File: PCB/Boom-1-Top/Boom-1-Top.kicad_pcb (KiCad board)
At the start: 4 copper layers, 345 x 165 mm, 770 parts, among them J1 DEBUG, J10 PIC_DEBUG, J11 PIC_DEBUG, J12 PIC_DEBUG, J13 PIC_DEBUG, J14 PIC_DEBUG, J15 USB_B_Micro, J16 SD_Card, J17 BT_DEBUG, J18 12V Supply, J19 3V3 Bypass, J2 MIDI IN, J20 5V Bypass, J3 MIDI OUT, J37 Osc1Conn, J38 Osc2Conn, J39 SubNoiseConn, J4 PIC_DEBUG, J40 FiltConn2, J41 EnvGenConn2, J42 EnvGenConn1, J43 FXConn1, J44 FiltConn1, J45 FXConn2, J46 EnvGenConn3, J5 PIC_DEBUG, J6 PIC_DEBUG, J7 PIC_DEBUG, J8 PIC_DEBUG, J9 PIC_DEBUG, Q1 AO3401A, Q2 AO3401A, SW1 Osc1SawEncoder, SW10 SubToOsc2FiltEncoder, SW11 Osc1ToOsc2FiltEncoder, SW12 Osc1FiltFreqEncoder, SW13 Osc2FiltFreqEncoder, SW14 SubFiltFreqEncoder, SW15 OscFiltEnvAttackEncoder, SW16 SubFiltEnvAttackEncoder, SW17 Osc1FiltResEncoder, SW18 Osc2FiltResEncoder, SW19 SubFiltResEncoder, SW2 Osc1SqrEncoder, SW20 OscFiltEnvDecayEncoder, SW21 SubFiltEnvDecayEncoder, SW22 OscFiltEnvSustainEncoder, SW23 SubFiltEnvSustainEncoder, SW24 Osc1DriveEncoder, SW25 Osc2DistortionEncoder, SW26 OscFiltEnvReleaseEncoder, SW27 SubFiltEnvReleaseEncoder, SW28 FXWetDryEncoder, SW29 SubAmpEnvAttackEncoder, SW3 Rotary_Encoder, SW30 OscAmpEnvAttackEncoder, SW31 FXControl1Encoder, SW32 SubAmpEnvDecayEncoder, SW33 OscAmpEnvDecayEncoder, SW34 FXControl2Encoder, SW35 SubAmpEnvSustainEncoder, SW36 OscAmpEnvSustainEncoder, SW37 FXControl3Encoder, SW38 FXFeedbackEncoder, SW39 SubAmpEnvReleaseEncoder, SW4 Rotary_Encoder_Switch, SW40 OscAmpEnvReleaseEncoder, SW41 Reset, SW43 Reset, SW5 Rotary_Encoder, SW53 Osc1TuneEncoder, SW6 SubToSubFiltEncoder, SW7 SubNoiseEncoder, U1 STM32F407VGTx, U10 DAC7678xPW, U11 PIC18F26Q43, U12 PIC18F26Q43, U13 PIC18F26Q43, U14 PIC18F26Q43, U15 PIC18F26Q43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

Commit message: Left-side knobs now all have 22mm spacing between them And 29mm between the groups
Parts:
- moved SW1 1.00 mm to (150.0, 107.2)
- moved SW7 1.00 mm to (150.0, 253.2)
- moved SW2 0.50 mm to (150.0, 129.2)
- moved SW3 0.50 mm to (150.0, 158.2)
- moved SW4 0.50 mm to (150.0, 180.2)
- moved SW5 0.50 mm to (150.0, 202.2)
- moved SW6 0.50 mm to (150.0, 231.2)
- moved SW28 0.20 mm to (378.0, 180.2)
- moved SW31 0.20 mm to (402.0, 180.2)
- moved SW34 0.20 mm to (422.0, 180.2)
- moved SW37 0.20 mm to (442.0, 180.2)

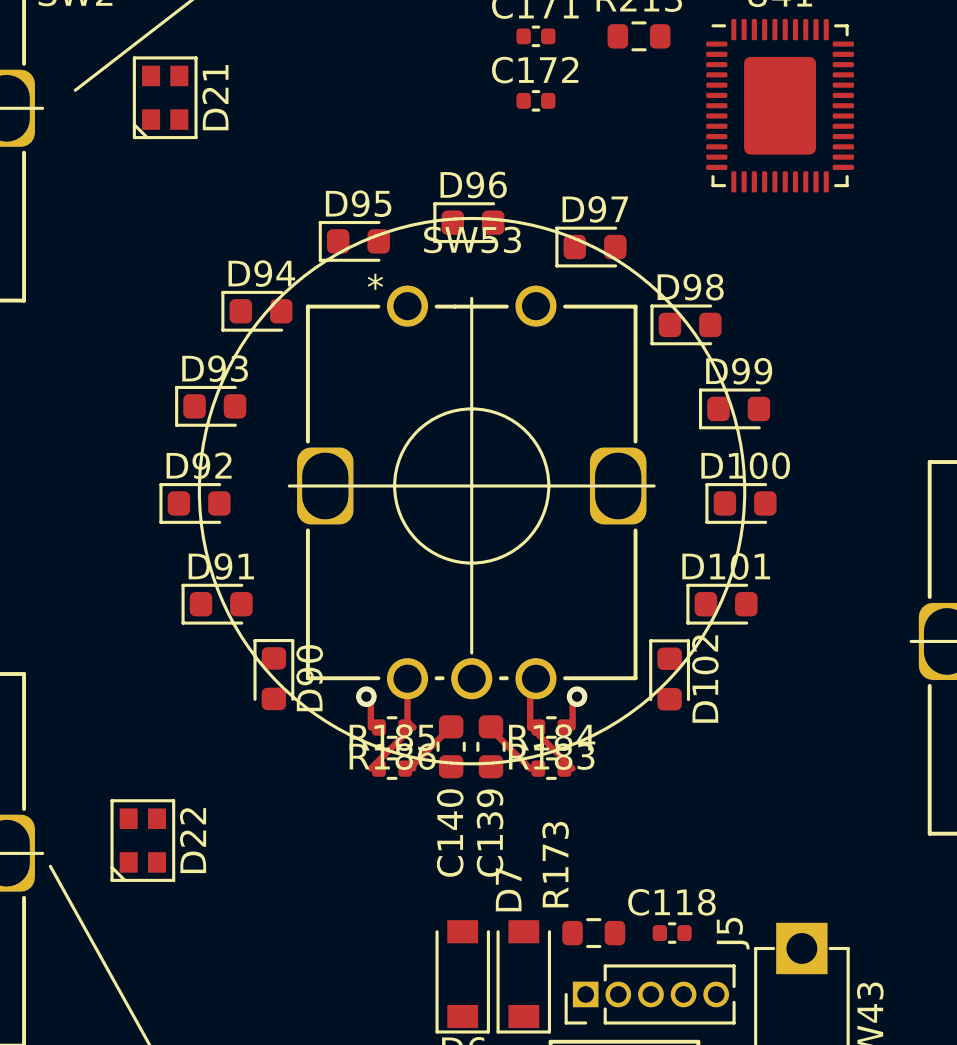
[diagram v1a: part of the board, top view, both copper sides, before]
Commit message: Re-aligned horizontal guide lines Aligned tune knob
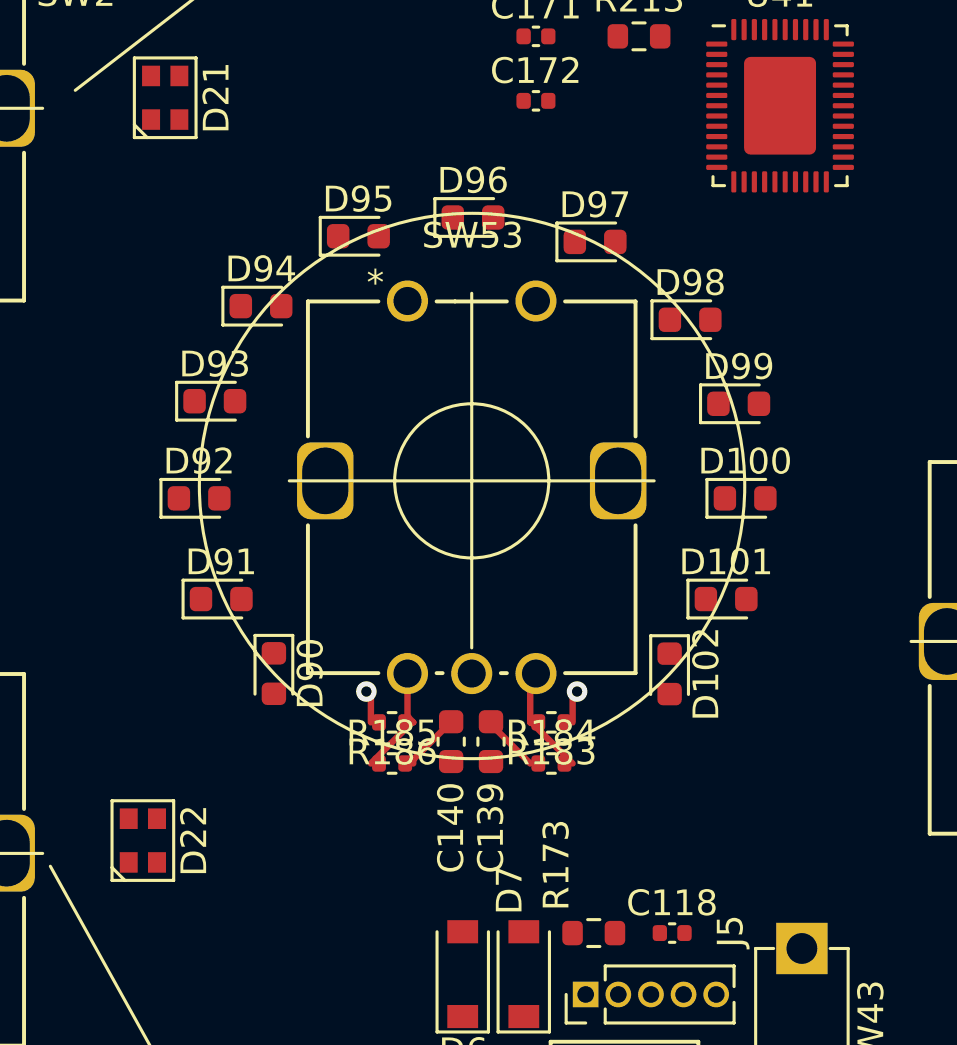
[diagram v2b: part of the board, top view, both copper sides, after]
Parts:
- moved C139 0.20 mm to (177.1, 160.8)
- moved C140 0.20 mm to (175.5, 160.8)
- moved D100 0.20 mm to (186.9, 151.4)
- moved D90 0.20 mm to (168.6, 158.2)
- moved D92 0.20 mm to (165.7, 151.4)
- moved D93 0.20 mm to (166.3, 147.6)
- moved D96 0.20 mm to (176.3, 140.4)
- moved D99 0.20 mm to (186.7, 147.7)
- moved R183 0.20 mm to (179.4, 160.1)
- moved R184 0.20 mm to (179.4, 161.7)
- moved R185 0.20 mm to (173.2, 161.7)
- moved R186 0.20 mm to (173.2, 160.1)
- moved SW53 0.20 mm to (173.8, 143.7)
- moved D101 0.20 mm to (186.2, 155.3)
- moved D102 0.20 mm to (184.0, 158.2)
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
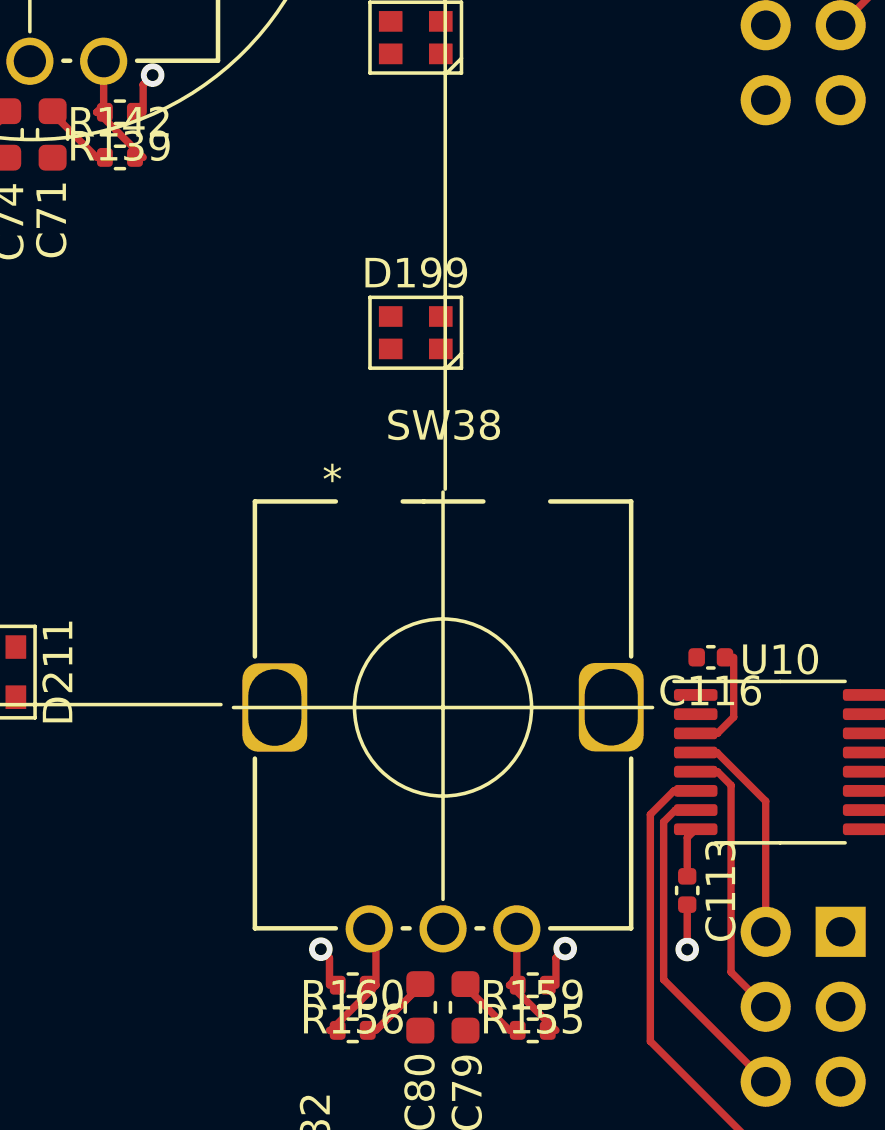
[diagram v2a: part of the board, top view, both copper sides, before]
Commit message: Fixed horizontal guide lines
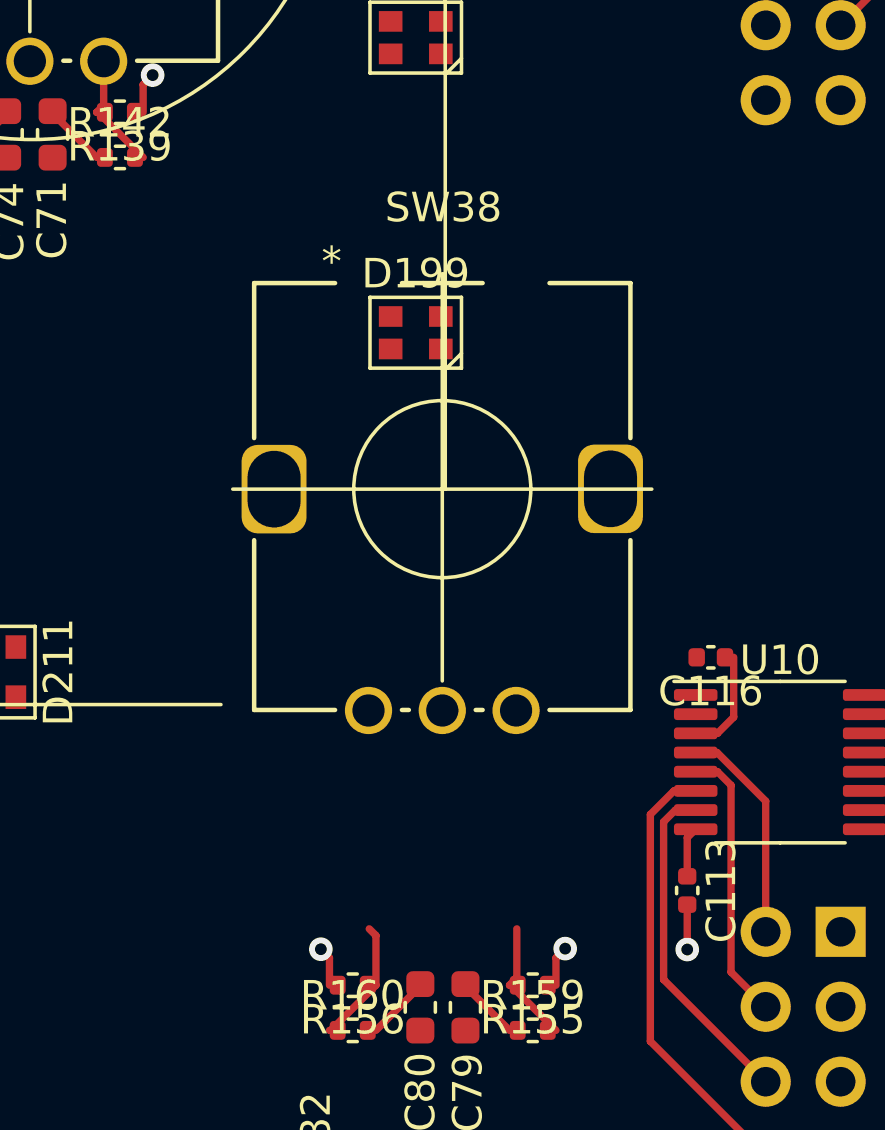
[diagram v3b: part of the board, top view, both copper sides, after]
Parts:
- moved SW38 7.40 mm to (456.0, 202.2)
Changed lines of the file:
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@@
   (general
     (thickness 1.6)
-    (drawings 88)
+    (drawings 93)
     (tracks 1239)
     (zones 0)
@@
     (38 B.Mask user)
     (39 F.Mask user)
-    (40 Dwgs.User user hide)
+    (40 Dwgs.User user)
     (41 Cmts.User user)
     (42 Eco1.User user)
@@
   )
   (module PEC11R:PEC11R-4x15F-N0024 locked (layer F.Cu)
-    (at 456.025 209.6)
+    (at 456 202.2)
     (fp_text reference SW38 (at 2.54 -2.54) (layer F.SilkS)
       (effects (font (size 1 1) (thickness 0.15)))
@@
     )
   )
+  (dimension 29 (width 0.15) (layer Dwgs.User)
+    (gr_text "29.000 mm" (at 449.5 201.7 270) (layer Dwgs.User)
+      (effects (font (size 1 1) (thickness 0.15)))
+    )
+    (feature1 (pts (xy 444.6 216.2) (xy 448.786421 216.2)))
+    (feature2 (pts (xy 444.6 187.2) (xy 448.786421 187.2)))
+    (crossbar (pts (xy 448.2 187.2) (xy 448.2 216.2)))
+    (arrow1a (pts (xy 448.2 216.2) (xy 447.613579 215.073496)))
+    (arrow1b (pts (xy 448.2 216.2) (xy 448.786421 215.073496)))
+    (arrow2a (pts (xy 448.2 187.2) (xy 447.613579 188.326504)))
+    (arrow2b (pts (xy 448.2 187.2) (xy 448.786421 188.326504)))
+  )
+  (dimension 22 (width 0.15) (layer Dwgs.User)
+    (gr_text "22.000 mm" (at 467.8 198.2 270) (layer Dwgs.User)
+      (effects (font (size 1 1) (thickness 0.15)))
+    )
+    (feature1 (pts (xy 444.6 209.2) (xy 467.086421 209.2)))
+    (feature2 (pts (xy 444.6 187.2) (xy 467.086421 187.2)))
+    (crossbar (pts (xy 466.5 187.2) (xy 466.5 209.2)))
+    (arrow1a (pts (xy 466.5 209.2) (xy 465.913579 208.073496)))
+    (arrow1b (pts (xy 466.5 209.2) (xy 467.086421 208.073496)))
+    (arrow2a (pts (xy 466.5 187.2) (xy 465.913579 188.326504)))
+    (arrow2b (pts (xy 466.5 187.2) (xy 467.086421 188.326504)))
+  )
+  (dimension 14.5 (width 0.15) (layer Dwgs.User)
+    (gr_text "14.500 mm" (at 162 157.95 90) (layer Dwgs.User)
+      (effects (font (size 1 1) (thickness 0.15)))
+    )
+    (feature1 (pts (xy 152.5 150.7) (xy 161.286421 150.7)))
+    (feature2 (pts (xy 152.5 165.2) (xy 161.286421 165.2)))
+    (crossbar (pts (xy 160.7 165.2) (xy 160.7 150.7)))
+    (arrow1a (pts (xy 160.7 150.7) (xy 161.286421 151.826504)))
+    (arrow1b (pts (xy 160.7 150.7) (xy 160.113579 151.826504)))
+    (arrow2a (pts (xy 160.7 165.2) (xy 161.286421 164.073496)))
+    (arrow2b (pts (xy 160.7 165.2) (xy 160.113579 164.073496)))
+  )
+  (dimension 14.5 (width 0.15) (layer Dwgs.User)
+    (gr_text "14.500 mm" (at 159.4 143.45 270) (layer Dwgs.User)
+      (effects (font (size 1 1) (thickness 0.15)))
+    )
+    (feature1 (pts (xy 160.7 150.7) (xy 160.113579 150.7)))
+    (feature2 (pts (xy 160.7 136.2) (xy 160.113579 136.2)))
+    (crossbar (pts (xy 160.7 136.2) (xy 160.7 150.7)))
+    (arrow1a (pts (xy 160.7 150.7) (xy 160.113579 149.573496)))
+    (arrow1b (pts (xy 160.7 150.7) (xy 161.286421 149.573496)))
+    (arrow2a (pts (xy 160.7 136.2) (xy 160.113579 137.326504)))
+    (arrow2b (pts (xy 160.7 136.2) (xy 161.286421 137.326504)))
+  )
+  (gr_line (start 184.5 150.7) (end 144.1 150.7) (layer Dwgs.User) (width 0.15))
+  (dimension 31 (width 0.15) (layer Dwgs.User)
+    (gr_text "31.000 mm" (at 227.3 233.7 270) (layer Dwgs.User)
+      (effects (font (size 1 1) (thickness 0.15)))
+    )
+    (feature1 (pts (xy 228.6 249.2) (xy 228.013579 249.2)))
+    (feature2 (pts (xy 228.6 218.2) (xy 228.013579 218.2)))
+    (crossbar (pts (xy 228.6 218.2) (xy 228.6 249.2)))
+    (arrow1a (pts (xy 228.6 249.2) (xy 228.013579 248.073496)))
+    (arrow1b (pts (xy 228.6 249.2) (xy 229.186421 248.073496)))
+    (arrow2a (pts (xy 228.6 218.2) (xy 228.013579 219.326504)))
+    (arrow2b (pts (xy 228.6 218.2) (xy 229.186421 219.326504)))
+  )
+  (dimension 31 (width 0.15) (layer Dwgs.User)
+    (gr_text "31.000 mm" (at 227.3 202.7 270) (layer Dwgs.User)
+      (effects (font (size 1 1) (thickness 0.15)))
+    )
+    (feature1 (pts (xy 236.5 218.2) (xy 228.013579 218.2)))
+    (feature2 (pts (xy 236.5 187.2) (xy 228.013579 187.2)))
+    (crossbar (pts (xy 228.6 187.2) (xy 228.6 218.2)))
+    (arrow1a (pts (xy 228.6 218.2) (xy 228.013579 217.073496)))
+    (arrow1b (pts (xy 228.6 218.2) (xy 229.186421 217.073496)))
+    (arrow2a (pts (xy 228.6 187.2) (xy 228.013579 188.326504)))
+    (arrow2b (pts (xy 228.6 187.2) (xy 229.186421 188.326504)))
+  )
+  (dimension 31 (width 0.15) (layer Dwgs.User)
+    (gr_text "31.000 mm" (at 229.9 140.7 90) (layer Dwgs.User)
+      (effects (font (size 1 1) (thickness 0.15)))
+    )
+    (feature1 (pts (xy 228.6 125.2) (xy 229.186421 125.2)))
+    (feature2 (pts (xy 228.6 156.2) (xy 229.186421 156.2)))
+    (crossbar (pts (xy 228.6 156.2) (xy 228.6 125.2)))
+    (arrow1a (pts (xy 228.6 125.2) (xy 229.186421 126.326504)))
+    (arrow1b (pts (xy 228.6 125.2) (xy 228.013579 126.326504)))
+    (arrow2a (pts (xy 228.6 156.2) (xy 229.186421 155.073496)))
+    (arrow2b (pts (xy 228.6 156.2) (xy 228.013579 155.073496)))
+  )
+  (dimension 31 (width 0.15) (layer Dwgs.User)
+    (gr_text "31.000 mm" (at 227.3 171.7 90) (layer Dwgs.User)
+      (effects (font (size 1 1) (thickness 0.15)))
+    )
+    (feature1 (pts (xy 236.5 156.2) (xy 228.013579 156.2)))
+    (feature2 (pts (xy 236.5 187.2) (xy 228.013579 187.2)))
+    (crossbar (pts (xy 228.6 187.2) (xy 228.6 156.2)))
+    (arrow1a (pts (xy 228.6 156.2) (xy 229.186421 157.326504)))
+    (arrow1b (pts (xy 228.6 156.2) (xy 228.013579 157.326504)))
+    (arrow2a (pts (xy 228.6 187.2) (xy 229.186421 186.073496)))
+    (arrow2b (pts (xy 228.6 187.2) (xy 228.013579 186.073496)))
+  )
   (dimension 11 (width 0.15) (layer Dwgs.User)
     (gr_text "11.000 mm" (at 162 254.7 90) (layer Dwgs.User)
@@
   (target plus (at 304 269.7) (size 5) (width 0.05) (layer Edge.Cuts))
   (gr_line (start 304 104.7) (end 304 269.7) (layer Dwgs.User) (width 0.12))
-  (dimension 141.7476 (width 0.12) (layer Dwgs.User)
-    (gr_text "141.748 mm" (at 398.3738 212.47) (layer Dwgs.User)
-      (effects (font (size 1 1) (thickness 0.15)))
-    )
-    (feature1 (pts (xy 469.2476 211.2) (xy 469.2476 211.786421)))
-    (feature2 (pts (xy 327.5 211.2) (xy 327.5 211.786421)))
-    (crossbar (pts (xy 327.5 211.2) (xy 469.2476 211.2)))
-    (arrow1a (pts (xy 469.2476 211.2) (xy 468.121096 211.786421)))
-    (arrow1b (pts (xy 469.2476 211.2) (xy 468.121096 210.613579)))
-    (arrow2a (pts (xy 327.5 211.2) (xy 328.626504 211.786421)))
-    (arrow2b (pts (xy 327.5 211.2) (xy 328.626504 210.613579)))
-  )
-  (dimension 141.2476 (width 0.12) (layer Dwgs.User)
-    (gr_text "141.248 mm" (at 402.6262 163.18) (layer Dwgs.User)
-      (effects (font (size 1 1) (thickness 0.15)))
-    )
-    (feature1 (pts (xy 473.25 164.5597) (xy 473.25 163.863579)))
-    (feature2 (pts (xy 332.0024 164.5597) (xy 332.0024 163.863579)))
-    (crossbar (pts (xy 332.0024 164.45) (xy 473.25 164.45)))
-    (arrow1a (pts (xy 473.25 164.45) (xy 472.123496 165.036421)))
-    (arrow1b (pts (xy 473.25 164.45) (xy 472.123496 163.863579)))
-    (arrow2a (pts (xy 332.0024 164.45) (xy 333.128904 165.036421)))
-    (arrow2b (pts (xy 332.0024 164.45) (xy 333.128904 163.863579)))
-  )
   (gr_line (start 368.5 136.7) (end 368.5 241.7) (layer Dwgs.User) (width 0.12))
   (gr_line (start 170 201.7) (end 170 267.95) (layer Dwgs.User) (width 0.12))
-  (gr_line (start 232 218.2) (end 337.75 218.2) (layer Dwgs.User) (width 0.12))
-  (gr_line (start 131.5 156.95) (end 336.25 156.95) (layer Dwgs.User) (width 0.12))
+  (gr_line (start 131.5 218.2) (end 476.5 218.2) (layer Dwgs.User) (width 0.12))
+  (gr_line (start 131.35 156.2) (end 476.5 156.2) (layer Dwgs.User) (width 0.12))
   (gr_line (start 131.5 249.2) (end 476.5 249.2) (layer Dwgs.User) (width 0.12))
   (gr_line (start 131.5 125.2) (end 476.5 125.2) (layer Dwgs.User) (width 0.12))
-  (dimension 7.25 (width 0.15) (layer Dwgs.User)
-    (gr_text "7.250 mm" (at 151.3 155.075 90) (layer Dwgs.User)
-      (effects (font (size 1 1) (thickness 0.15)))
-    )
-    (feature1 (pts (xy 150 151.45) (xy 150.586421 151.45)))
-    (feature2 (pts (xy 150 158.7) (xy 150.586421 158.7)))
-    (crossbar (pts (xy 150 158.7) (xy 150 151.45)))
-    (arrow1a (pts (xy 150 151.45) (xy 150.586421 152.576504)))
-    (arrow1b (pts (xy 150 151.45) (xy 149.413579 152.576504)))
-    (arrow2a (pts (xy 150 158.7) (xy 150.586421 157.573496)))
-    (arrow2b (pts (xy 150 158.7) (xy 149.413579 157.573496)))
-  )
-  (dimension 7.25 (width 0.15) (layer Dwgs.User)
-    (gr_text "7.250 mm" (at 148.7 147.825 270) (layer Dwgs.User)
-      (effects (font (size 1 1) (thickness 0.15)))
-    )
-    (feature1 (pts (xy 150 151.45) (xy 149.413579 151.45)))
-    (feature2 (pts (xy 150 144.2) (xy 149.413579 144.2)))
-    (crossbar (pts (xy 150 144.2) (xy 150 151.45)))
-    (arrow1a (pts (xy 150 151.45) (xy 149.413579 150.323496)))
-    (arrow1b (pts (xy 150 151.45) (xy 150.586421 150.323496)))
-    (arrow2a (pts (xy 150 144.2) (xy 149.413579 145.326504)))
-    (arrow2b (pts (xy 150 144.2) (xy 150.586421 145.326504)))
-  )
   (gr_line (start 131.5 136.2) (end 476.5 136.2) (layer Dwgs.User) (width 0.12))
   (gr_line (start 131.5 238.2) (end 476.5 238.2) (layer Dwgs.User) (width 0.12))

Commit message: FX alt1
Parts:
- moved C67 22.2 mm to (425.2, 219.4)
- moved C68 22.2 mm to (423.6, 219.4)
- moved D193 22.2 mm to (414.5, 208.3)
- moved D197 22.2 mm to (454.7, 210.3)
- moved D326 22.2 mm to (434.4, 208.3)
- moved R122 22.2 mm to (407.4, 220.1)
- moved R123 22.2 mm to (401.4, 220.1)
- moved R133 22.2 mm to (427.5, 218.6)
- moved R136 22.2 mm to (421.4, 218.6)
- moved SW31 22.2 mm to (401.9, 202.4)
- moved SW34 22.2 mm to (421.9, 202.4)
- moved SW37 22.2 mm to (441.9, 202.4)
- moved SW38 22.2 mm to (455.9, 224.4)
- moved C61 22.2 mm to (405.2, 219.3)
- moved C63 22.2 mm to (403.7, 219.3)
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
